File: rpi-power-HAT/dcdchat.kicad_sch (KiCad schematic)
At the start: 22 parts

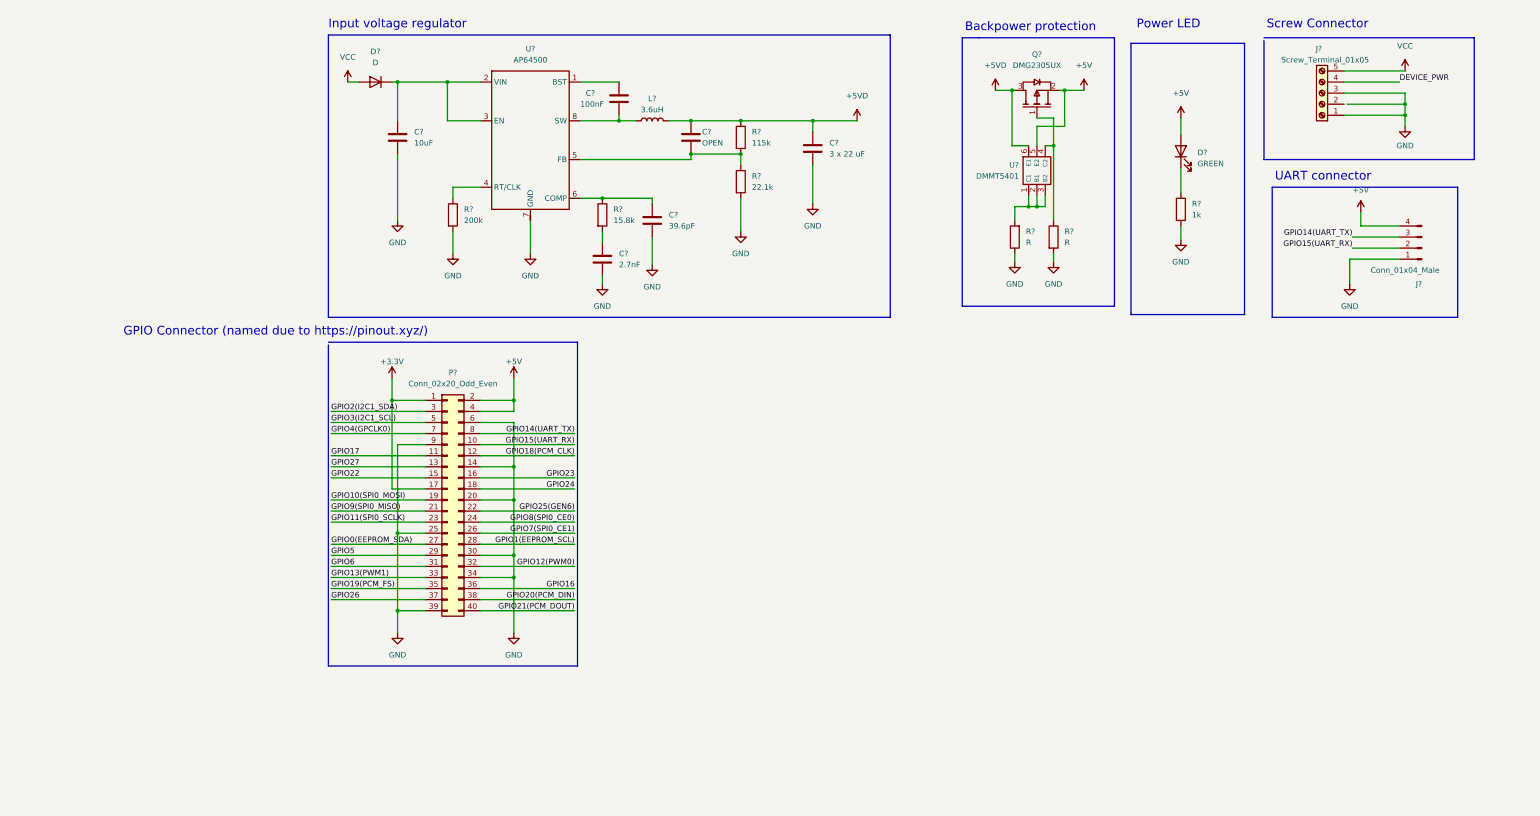
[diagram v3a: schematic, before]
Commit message: Added schematic for connector. Added diode to protect from wrong polarity  . Added footprintlibrary for AP64500
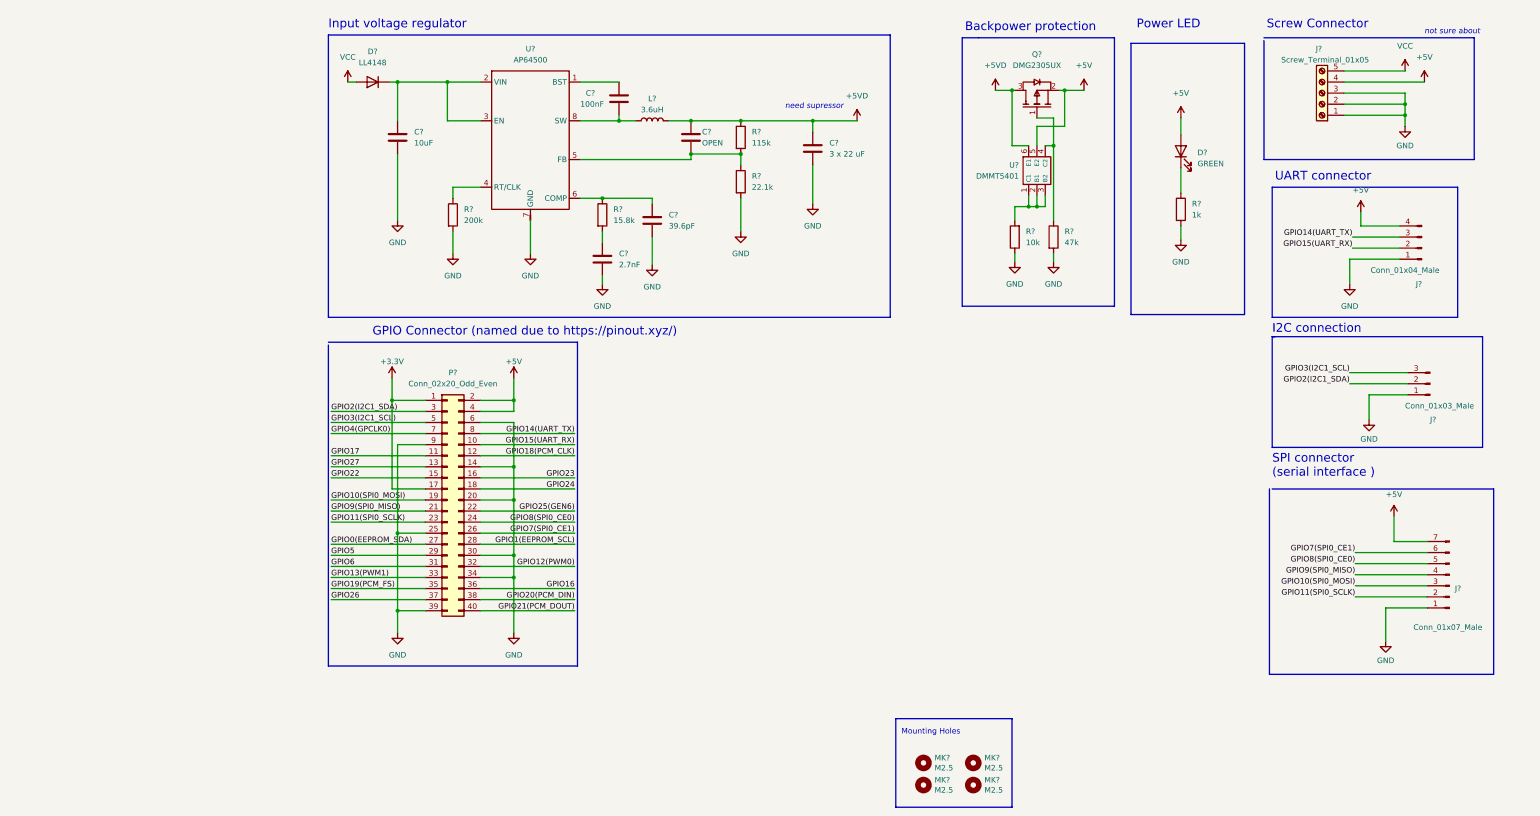
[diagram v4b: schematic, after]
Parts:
- removed D?: D, symbol Device:D
- added D?: LL4148, Diode_SMD:D_MiniMELF, symbol Diode:LL4148
- added J?: Conn_01x07_Male, symbol Connector:Conn_01x07_Male
- added J?: Conn_01x03_Male, symbol Connector:Conn_01x03_Male
- added MK? (x4): M2.5, MountingHole:MountingHole_2.7mm_M2.5_Pad, symbol Mechanical:MountingHole
- R?: value R -> 10k
- R?: value R -> 47k
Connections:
- net DEVICE_PWR is gone; now on net +5V: J?.4 (Pin_4)
- net +5V: now also J?.7 (Pin_7)
- net GND: now also J?.2 (Pin_2), J?.1 (Pin_1), J?.1 (Pin_1)
- net GPIO10(SPI0_MOSI): now also J?.3 (Pin_3)
- net GPIO11(SPI0_SCLK): now also J?.2 (Pin_2)
- net GPIO2(I2C1_SDA): now also J?.2 (Pin_2)
- net GPIO3(I2C1_SCL): now also J?.3 (Pin_3)
- net GPIO7(SPI0_CE1): now also J?.6 (Pin_6)
- net GPIO8(SPI0_CE0): now also J?.5 (Pin_5)
- net GPIO9(SPI0_MISO): now also J?.4 (Pin_4)
- net VCC: now also D?.2 (A)
- net at C?.1, U?.2 (VIN), U?.3 (EN): now also D?.1 (K)
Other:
- note added: "I2C connection"
- note added: "Mounting Holes"
- note added: "SPI connector (serial interface )"
- note added: "need supressor"
- note added: "not sure about"

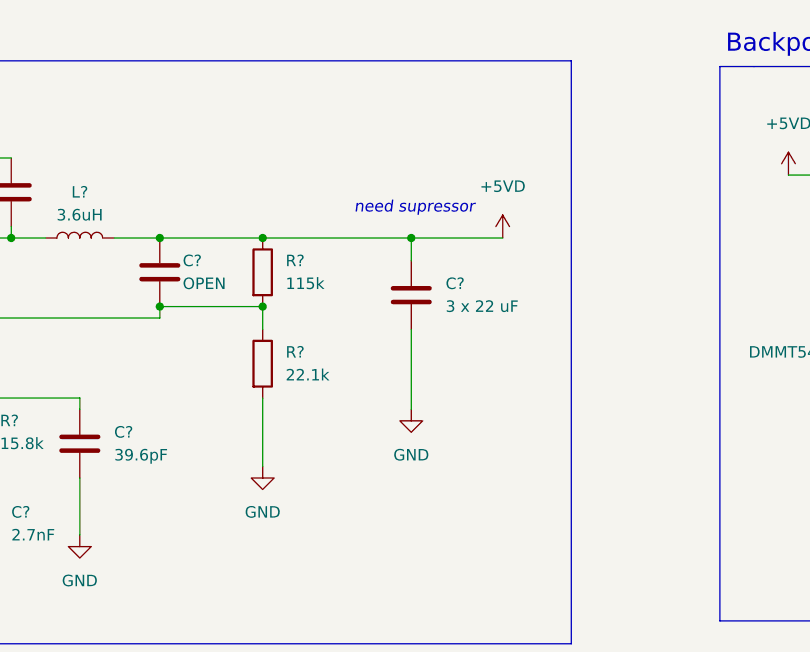
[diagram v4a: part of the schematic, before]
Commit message: Added TVS-diode
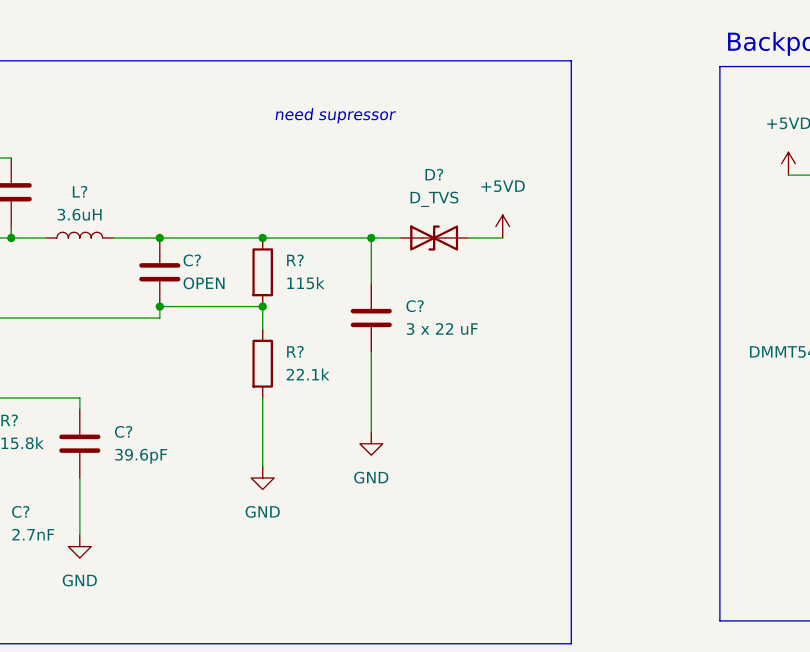
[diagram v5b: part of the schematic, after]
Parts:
- added D?: D_TVS, symbol Device:D_TVS
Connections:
- net +5VD: now also D?.2 (A2); no longer C?.1, C?.1, L?.2, R?.1
- new net: C?.1, C?.1, D?.1 (A1), L?.2, R?.1
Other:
- moved on the sheet: C?
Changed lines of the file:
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@@
   (junction (at 43.815 28.575) (diameter 0) (color 0 0 0 0)
   )
-  (junction (at 127.635 37.465) (diameter 0) (color 0 0 0 0)
-  )
   (junction (at 99.695 37.465) (diameter 0) (color 0 0 0 0)
   )
@@
   (junction (at 111.125 37.465) (diameter 0) (color 0 0 0 0)
   )
+  (junction (at 123.19 37.465) (diameter 0) (color 0 0 0 0)
+  )
   (junction (at 83.185 37.465) (diameter 0) (color 0 0 0 0)
   )
@@
     (stroke (width 0) (type default) (color 0 0 0 0))
   )
-  (wire (pts (xy 111.125 37.465) (xy 127.635 37.465))
+  (wire (pts (xy 111.125 37.465) (xy 123.19 37.465))
     (stroke (width 0) (type default) (color 0 0 0 0))
   )
@@
     (stroke (width 0) (type default) (color 0 0 0 0))
   )
-  (wire (pts (xy 127.635 47.625) (xy 127.635 56.515))
+  (wire (pts (xy 123.19 50.165) (xy 123.19 59.055))
     (stroke (width 0) (type default) (color 0 0 0 0))
   )
@@
     (stroke (width 0) (type default) (color 0 0 0 0))
   )
-  (wire (pts (xy 127.635 37.465) (xy 127.635 40.005))
+  (wire (pts (xy 123.19 37.465) (xy 123.19 42.545))
     (stroke (width 0) (type default) (color 0 0 0 0))
   )
@@
     (stroke (width 0) (type default) (color 0 0 0 0))
   )
+  (wire (pts (xy 133.985 37.465) (xy 137.795 37.465))
+    (stroke (width 0) (type default) (color 0 0 0 0))
+  )
   (wire (pts (xy 51.435 129.54) (xy 73.025 129.54))
     (stroke (width 0) (type default) (color 0 0 0 0))
@@
     (stroke (width 0) (type default) (color 0 0 0 0))
   )
-  (wire (pts (xy 127.635 37.465) (xy 137.795 37.465))
-    (stroke (width 0) (type default) (color 0 0 0 0))
-  )
   (wire (pts (xy 51.435 139.7) (xy 73.025 139.7))
     (stroke (width 0) (type default) (color 0 0 0 0))
@@
   )
   (wire (pts (xy 180.975 57.15) (xy 180.975 54.61))
+    (stroke (width 0) (type default) (color 0 0 0 0))
+  )
+  (wire (pts (xy 123.19 37.465) (xy 126.365 37.465))
     (stroke (width 0) (type default) (color 0 0 0 0))
   )
@@
     (effects (font (size 1.27 1.27) italic) (justify left bottom))
   )
-  (text "need supressor" (at 121.285 34.925 0)
+  (text "need supressor" (at 112.395 24.765 0)
     (effects (font (size 1.27 1.27) italic) (justify left bottom))
   )
@@
     (pin "1")
   )
-  (symbol (lib_id "power:GND") (at 127.635 56.515 0) (unit 1)
-    (in_bom yes) (on_board yes) (fields_autoplaced)
-    (property "Reference" "#PWR?" (id 0) (at 127.635 62.865 0)
-      (effects (font (size 1.27 1.27)) hide)
-    )
-    (property "Value" "GND" (id 1) (at 127.635 61.595 0))
-    (property "Footprint" "" (id 2) (at 127.635 56.515 0)
-      (effects (font (size 1.27 1.27)) hide)
-    )
-    (property "Datasheet" "" (id 3) (at 127.635 56.515 0)
+  (symbol (lib_id "power:GND") (at 123.19 59.055 0) (unit 1)
+    (in_bom yes) (on_board yes) (fields_autoplaced)
+    (property "Reference" "#PWR?" (id 0) (at 123.19 65.405 0)
+      (effects (font (size 1.27 1.27)) hide)
+    )
+    (property "Value" "GND" (id 1) (at 123.19 64.135 0))
+    (property "Footprint" "" (id 2) (at 123.19 59.055 0)
+      (effects (font (size 1.27 1.27)) hide)
+    )
+    (property "Datasheet" "" (id 3) (at 123.19 59.055 0)
       (effects (font (size 1.27 1.27)) hide)
     )
@@
     (pin "3")
   )
-  (symbol (lib_id "Device:C") (at 127.635 43.815 0) (unit 1)
-    (in_bom yes) (on_board yes) (fields_autoplaced)
-    (property "Reference" "C?" (id 0) (at 131.445 42.5449 0)
-      (effects (font (size 1.27 1.27)) (justify left))
-    )
-    (property "Value" "3 x 22 uF" (id 1) (at 131.445 45.0849 0)
-      (effects (font (size 1.27 1.27)) (justify left))
-    )
-    (property "Footprint" "" (id 2) (at 128.6002 47.625 0)
-      (effects (font (size 1.27 1.27)) hide)
-    )
-    (property "Datasheet" "~" (id 3) (at 127.635 43.815 0)
+  (symbol (lib_id "Device:C") (at 123.19 46.355 0) (unit 1)
+    (in_bom yes) (on_board yes) (fields_autoplaced)
+    (property "Reference" "C?" (id 0) (at 127 45.0849 0)
+      (effects (font (size 1.27 1.27)) (justify left))
+    )
+    (property "Value" "3 x 22 uF" (id 1) (at 127 47.6249 0)
+      (effects (font (size 1.27 1.27)) (justify left))
+    )
+    (property "Footprint" "" (id 2) (at 124.1552 50.165 0)
+      (effects (font (size 1.27 1.27)) hide)
+    )
+    (property "Datasheet" "~" (id 3) (at 123.19 46.355 0)
       (effects (font (size 1.27 1.27)) hide)
     )
@@
     (pin "1")
   )
+  (symbol (lib_id "Device:D_TVS") (at 130.175 37.465 0) (unit 1)
+    (in_bom yes) (on_board yes) (fields_autoplaced)
+    (property "Reference" "D?" (id 0) (at 130.175 30.48 0))
+    (property "Value" "D_TVS" (id 1) (at 130.175 33.02 0))
+    (property "Footprint" "" (id 2) (at 130.175 37.465 0)
+      (effects (font (size 1.27 1.27)) hide)
+    )
+    (property "Datasheet" "~" (id 3) (at 130.175 37.465 0)
+      (effects (font (size 1.27 1.27)) hide)
+    )
+    (pin "1")
+    (pin "2")
+  )
   (symbol (lib_id "power:+5V") (at 253.365 58.42 0) (unit 1)
     (in_bom yes) (on_board yes) (fields_autoplaced)
@@
       (reference "D?") (unit 1) (value "LL4148") (footprint "Diode_SMD:D_MiniMELF")
     )
+    (path "/d965a4f9-978c-4a7f-b394-fb5326459717"
+      (reference "D?") (unit 1) (value "D_TVS") (footprint "")
+    )
     (path "/4cd9e473-2eb2-4377-b60b-c6c94e023542"

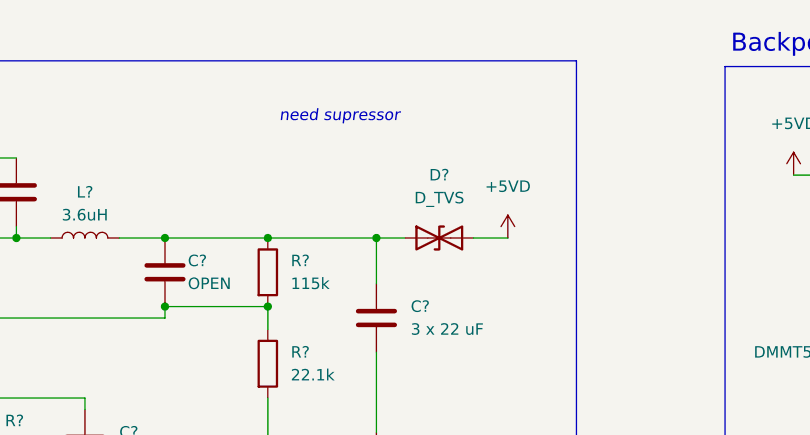
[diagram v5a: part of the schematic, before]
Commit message: Added footprints for elements
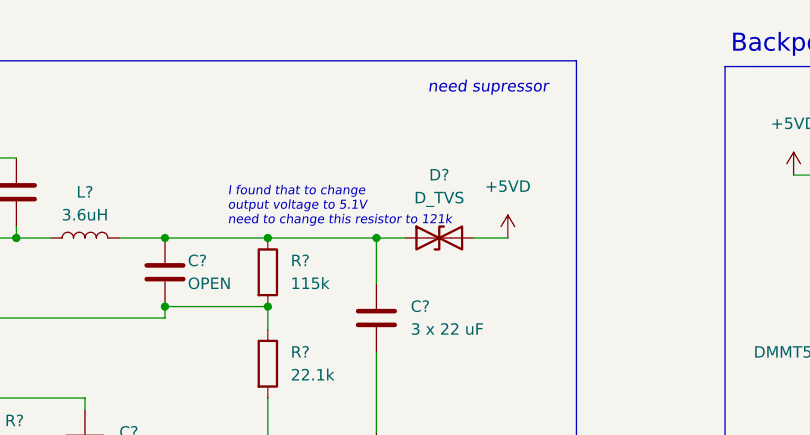
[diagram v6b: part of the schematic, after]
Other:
- note added: "I found that to change output voltage to 5.1V need to change this resistor to 121k"
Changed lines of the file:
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@@
     (effects (font (size 2 2)) (justify left bottom))
+  )
+  (text "I found that to change\noutput voltage to 5.1V\nneed to change this resistor to 121k"
+    (at 106.68 36.195 0)
+    (effects (font (size 1 1) italic) (justify left bottom))
   )
   (text "not sure about" (at 267.97 17.78 0)
     (effects (font (size 1.27 1.27) italic) (justify left bottom))
   )
-  (text "need supressor" (at 112.395 24.765 0)
+  (text "need supressor" (at 128.905 21.59 0)
     (effects (font (size 1.27 1.27) italic) (justify left bottom))
   )
